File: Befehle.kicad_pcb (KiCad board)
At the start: 2 copper layers, 60 parts, among them J1 2PinTerminalBlocktg, J2 2PinTerminalBlocktg, J3 3PinTerminalBlocktg, J4 2PinTerminalBlocktg, J5 2PinTerminalBlocktg, P1 CONN_02X10, P2 CONN_02X10, U1 74LS14, U2 74540, U3 7400, U4 74HCT02, U5 74LS541, U6 74LS373, U7 74LS139, U8 74LS540

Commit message: tracks gelegt und so
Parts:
- moved R8 77.0 mm to (71.0, 109.0), turned to 0 degrees
- moved R2 76.1 mm to (146.0, 148.5)
- moved D3 1.80 mm to (73.5, 113.0), turned to 180 degrees
- moved P1 1.77 mm to (50.8, 171.8)
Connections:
- P1 pad 10: Net-(P1-Pad10) -> GND
- P1 pad 11: Net-(P1-Pad11) -> GND
- P1 pad 12: GND -> /d2
- P1 pad 13: Net-(P1-Pad13) -> /d1
- P1 pad 14: Net-(P1-Pad14) -> /d2
- P1 pad 15: Net-(P1-Pad15) -> /d3
- P1 pad 16: Net-(P1-Pad16) -> /d4
- P1 pad 3: Net-(P1-Pad3) -> GND
- P1 pad 4: Net-(P1-Pad4) -> GND
- P1 pad 5: Net-(P1-Pad5) -> GND
- P1 pad 6: Net-(P1-Pad6) -> GND
- P1 pad 7: Net-(P1-Pad7) -> GND
- P1 pad 8: Net-(P1-Pad8) -> GND
- P1 pad 9: Net-(P1-Pad9) -> GND
- U5 pad 7: /a6 -> /a4
- U6 pad 11: Net-(U6-Pad11) -> Net-(R8-Pad2)
- U6 pad 15: /a3 -> /a4
- U6 pad 16: Net-(U6-Pad16) -> /a8
- U6 pad 19: Net-(U6-Pad19) -> /a2
- U6 pad 2: /a8 -> /a1
- U6 pad 3: /11 -> /d2
- U6 pad 5: /a7 -> /a3
- U6 pad 6: /a6 -> /a5
- U6 pad 9: /a5 -> /a7
- U7 pad 2: Net-(U6-Pad19) -> /a7
- U7 pad 3: Net-(U6-Pad16) -> /a4
- U8 pad 4: /a6 -> /a4
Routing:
- net GND: track 453.5 -> 565.5 mm, vias 0 -> 2
- net loadIR: track 22.8 -> 100.2 mm, vias 0 -> 2
- net Net-(R8-Pad2): track 0.00 -> 66.4 mm
- net /a4: track 80.4 -> 144.2 mm, vias 0 -> 2
- net /a6: track 41.1 -> 0.00 mm, vias 2 -> 0
- net /a5: track 49.3 -> 76.2 mm
- net /a3: track 67.8 -> 91.1 mm
- net /a1: track 87.5 -> 104.0 mm
- net /d2: track 17.1 -> 33.2 mm
- net /a8: track 58.8 -> 74.7 mm
- net /a2: track 77.9 -> 89.6 mm
- net Net-(D3-Pad2): track 0.00 -> 4.02 mm
- net /d3: track 36.9 -> 33.4 mm
- net /a7: track 86.8 -> 90.1 mm

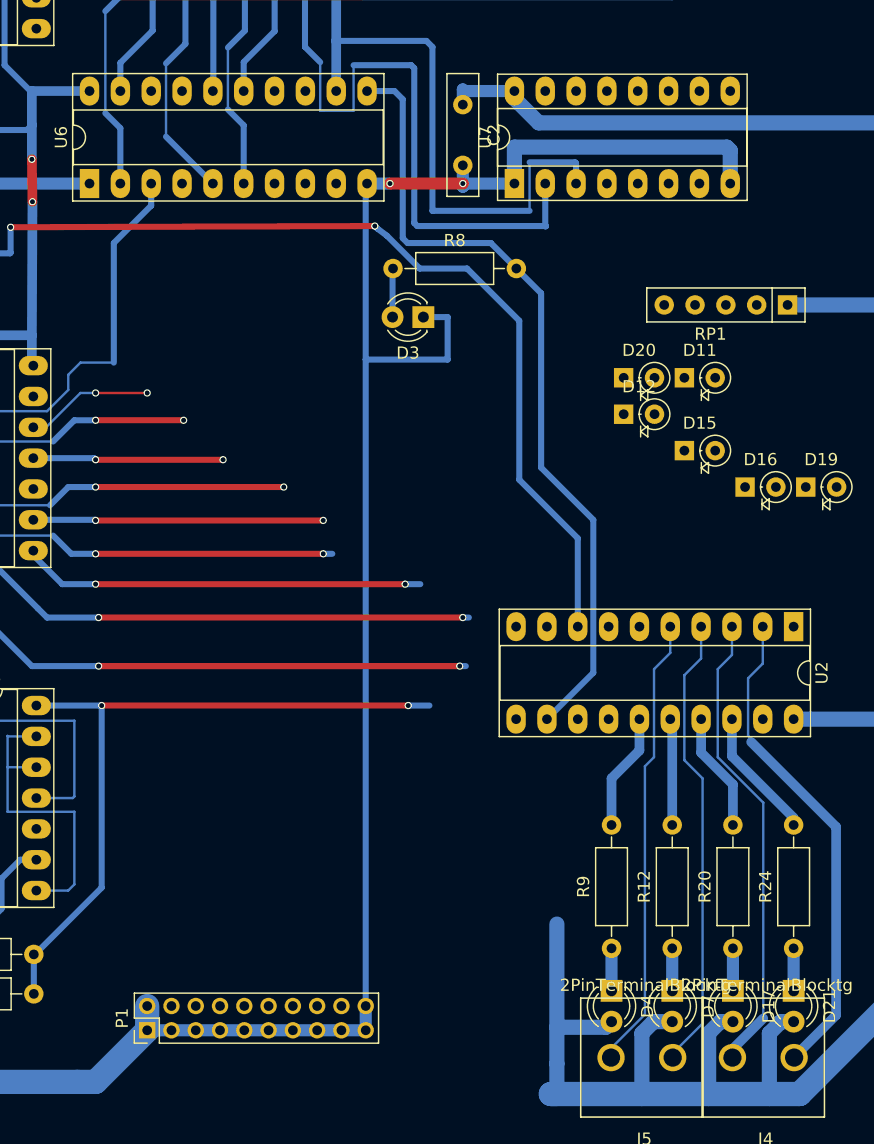
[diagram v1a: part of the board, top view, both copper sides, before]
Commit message: todos done (netze entflechten), some footprintslocaliszed
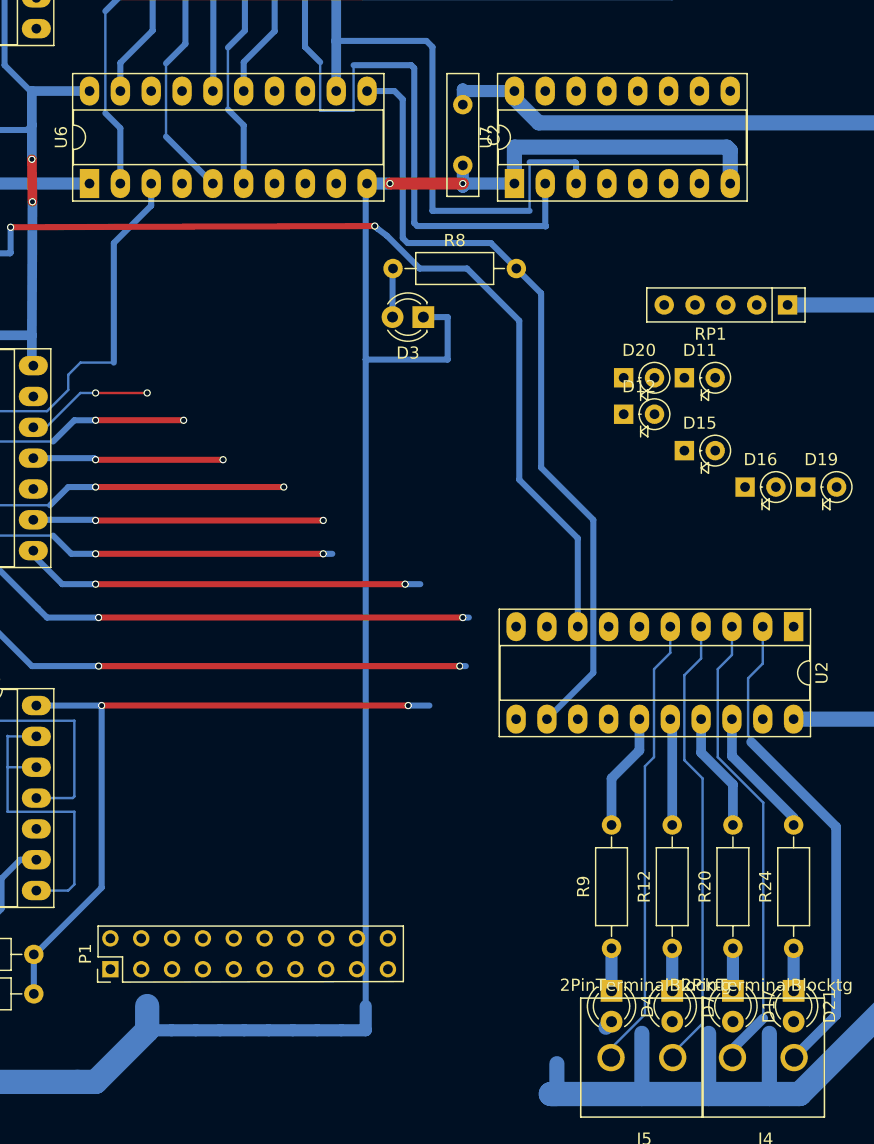
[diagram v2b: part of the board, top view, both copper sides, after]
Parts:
- U1, U3, U4: footprint Housings_DIP:DIP-14_W7.62mm_Socket_LongPads -> tg_foodprint:DIP-14_W7.62mm_Socket_LongPadstg
- U2, U5, U6, U8: footprint Housings_DIP:DIP-20_W7.62mm_Socket_LongPads -> tg_foodprint:DIP-20_W7.62mm_Socket_LongPadstg
- U7: footprint Housings_DIP:DIP-16_W7.62mm_Socket_LongPads -> tg_foodprint:DIP-16_W7.62mm_Socket_LongPadstg
- moved P1 5.87 mm to (47.7, 166.7)
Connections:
- P1 pad 12: /d2 -> (no net)
- P2 pad 11: Net-(P2-Pad11) -> (no net)
- P2 pad 12: Net-(P2-Pad12) -> (no net)
- P2 pad 13: Net-(P2-Pad13) -> (no net)
- P2 pad 14: Net-(P2-Pad14) -> (no net)
- P2 pad 15: Net-(P2-Pad15) -> (no net)
- P2 pad 16: Net-(P2-Pad16) -> (no net)
- P2 pad 17: Net-(P2-Pad17) -> (no net)
- P2 pad 18: Net-(P2-Pad18) -> (no net)
- U1 pad 8: Net-(U1-Pad8) -> (no net)
- U4 pad 10: Net-(U4-Pad10) -> (no net)
- U4 pad 11: /11 -> (no net)
- U4 pad 13: Net-(U4-Pad13) -> (no net)
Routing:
- net /11: track 15.7 -> 0.00 mm, vias 2 -> 0
- net (no net): track 0.00 -> 15.7 mm, vias 0 -> 2
- net VCC: track 607.2 -> 591.6 mm
- net Net-(D17-Pad2): track 8.31 -> 0.65 mm

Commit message: wires gelegt und schamdoozels beseitigt
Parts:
- moved R2 122.5 mm to (25.1, 129.3), turned to 270 degrees
- moved P1 5.20 mm to (45.8, 171.6)
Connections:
- J3 pad 2: incPCz -> incPC
- P1 pad 12: (no net) -> /d2
- P1 pad 14: /d2 -> /d7
- P1 pad 16: /d4 -> /d44
- P1 pad 19: /d7 -> /d4
- P2 pad 11: (no net) -> Net-(P2-Pad11)
- P2 pad 12: (no net) -> Net-(P2-Pad12)
- P2 pad 13: (no net) -> Net-(P2-Pad13)
- P2 pad 14: (no net) -> Net-(P2-Pad14)
- P2 pad 15: (no net) -> Net-(P2-Pad15)
- P2 pad 16: (no net) -> Net-(P2-Pad16)
- P2 pad 17: (no net) -> Net-(P2-Pad17)
- P2 pad 18: (no net) -> Net-(P2-Pad18)
- R3 pad 1: incPCz -> incPC
- R7 pad 1: Net-(R7-Pad1) -> incPC
- U1 pad 8: (no net) -> Net-(U1-Pad8)
- U2 pad 9: Net-(R7-Pad1) -> incPC
- U3 pad 1: incPCz -> incPC
- U3 pad 10: Net-(U3-Pad10) -> incPC
- U3 pad 2: incPCz -> incPC
- U3 pad 3: Net-(U3-Pad3) -> incPC
- U3 pad 4: Net-(R7-Pad1) -> incPC
- U3 pad 5: Net-(U3-Pad3) -> incPC
- U3 pad 6: Net-(U3-Pad10) -> incPC
- U4 pad 1: Net-(R7-Pad1) -> incPC
- U4 pad 10: (no net) -> incPC
- U4 pad 11: (no net) -> /d3
- U4 pad 12: /d7 -> /d1
- U4 pad 13: (no net) -> incPC
- U4 pad 3: /d1 -> /d7
- U4 pad 4: Net-(R7-Pad1) -> incPC
- U4 pad 5: /d4 -> /d44
- U4 pad 6: /d3 -> /d6
- U4 pad 8: /d6 -> /d4
- U6 pad 14: /d3 -> /d5
- U6 pad 17: /d2 -> /d3
- U6 pad 7: /d6 -> /d44
- U6 pad 8: /d5 -> /d6
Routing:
- net incPC: track 28.6 -> 225.0 mm, vias 0 -> 2
- net /d44: track 0.00 -> 94.2 mm, vias 0 -> 2
- net /d7: track 9.91 -> 88.0 mm
- net /d4: track 29.4 -> 103.1 mm
- net /d5: track 23.9 -> 95.7 mm
- net Net-(R7-Pad1): track 70.1 -> 0.00 mm, vias 2 -> 0
- net /d6: track 33.2 -> 98.3 mm
- net /d1: track 21.2 -> 85.7 mm
- net Net-(D1-Pad1): track 66.1 -> 3.32 mm, vias 4 -> 0
- net Net-(R2-Pad2): track 0.00 -> 59.1 mm, vias 0 -> 2
- net /d3: track 33.4 -> 91.5 mm
- net /d2: track 33.2 -> 85.6 mm
- net VCC: track 591.6 -> 625.6 mm
- net (no net): track 15.7 -> 0.00 mm, vias 2 -> 0
- net GND: track 565.5 -> 581.0 mm, vias 2 -> 4
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
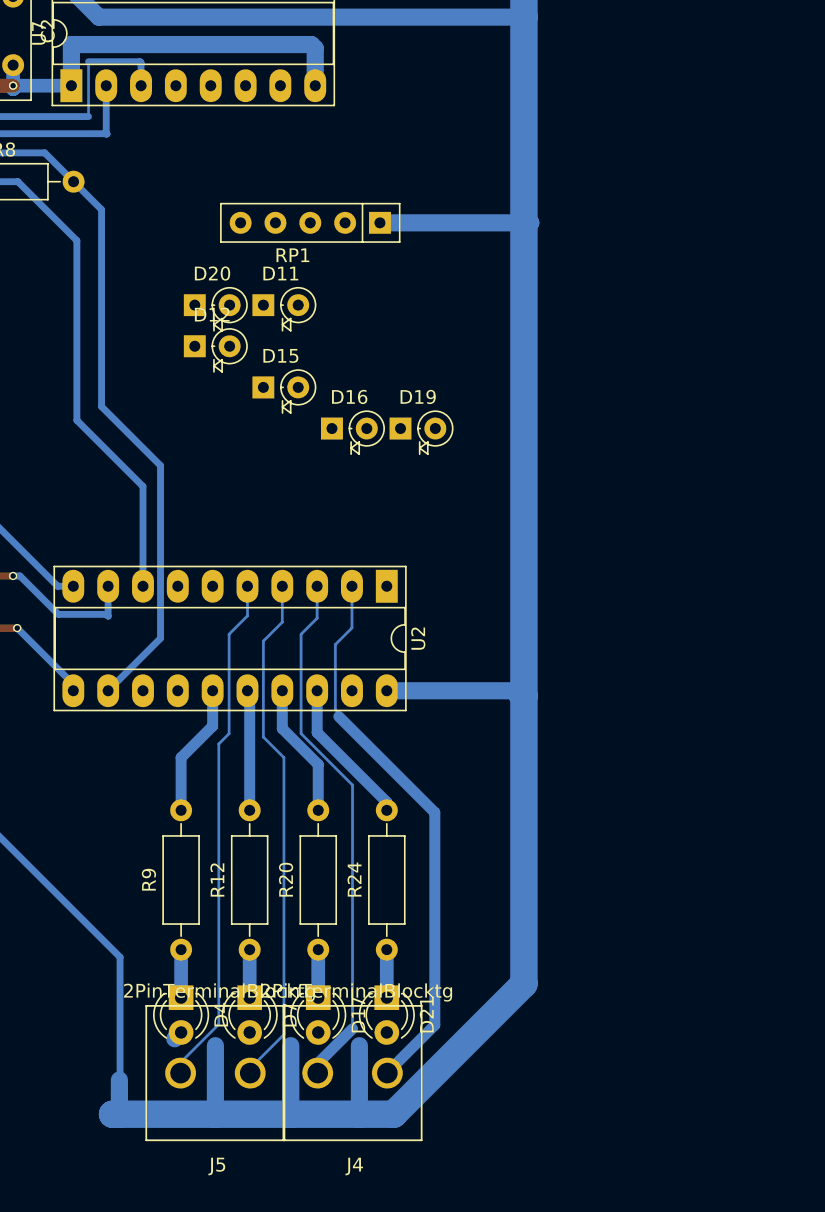
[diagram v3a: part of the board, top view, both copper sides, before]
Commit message: wires gelegt footprints getauscht
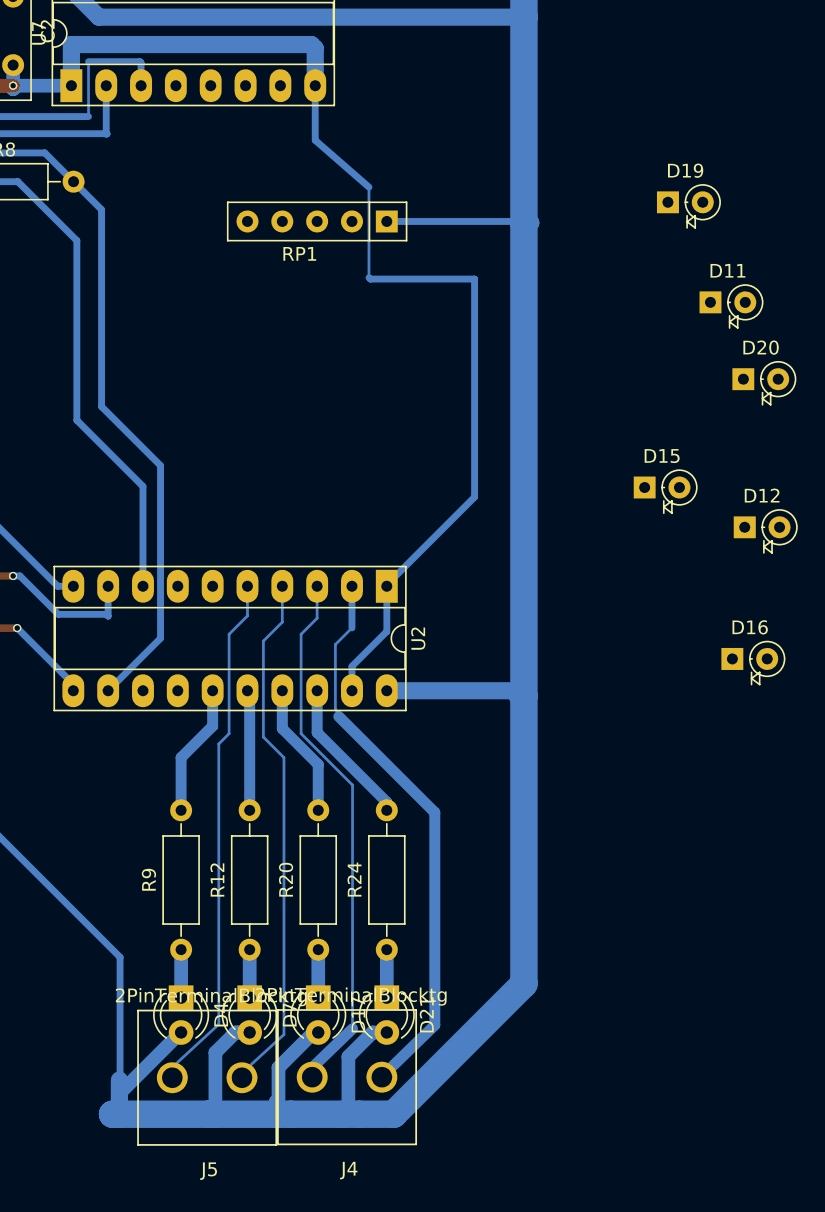
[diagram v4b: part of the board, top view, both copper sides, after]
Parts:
- moved D12 42.2 mm to (130.1, 134.2)
- moved D20 40.4 mm to (130.0, 123.4)
- moved D16 33.7 mm to (129.2, 143.8)
- moved D11 32.6 mm to (127.6, 117.8)
- moved D15 28.7 mm to (122.8, 131.3)
- moved D19 25.5 mm to (124.5, 110.5)
- moved J5 0.69 mm to (90.9, 174.3)
- moved RP1 0.51 mm to (104.0, 111.9)
- moved J4 0.50 mm to (101.1, 174.3)
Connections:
- D17 pad 2: Net-(D17-Pad2) -> VCC
- D21 pad 2: Net-(D17-Pad2) -> VCC
- D4 pad 2: Net-(D17-Pad2) -> VCC
- D7 pad 2: Net-(D17-Pad2) -> VCC
- U2 pad 15: Net-(R9-Pad2) -> Net-(R24-Pad2)
- U2 pad 16: VCC -> Net-(R20-Pad2)
- U2 pad 17: Net-(R20-Pad2) -> VCC
- U2 pad 18: Net-(R24-Pad2) -> Net-(R9-Pad2)
- U2 pad 2: 0 -> 3
- U2 pad 3: 1 -> 2
- U2 pad 4: 2 -> 1
- U2 pad 5: 3 -> 0
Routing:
- net GND: track 581.0 -> 638.3 mm
- net VCC: track 625.6 -> 644.1 mm
- net 2: track 37.7 -> 38.4 mm
- net 3: track 37.5 -> 38.2 mm
- net Net-(D17-Pad2): track 0.65 -> 0.00 mm
- net 1: track 38.6 -> 39.1 mm
- net 0: track 40.4 -> 41.0 mm

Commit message: lololol fertig gg ez
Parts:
- D11, D12, D15, D16, D19, D20: footprint Diodes_ThroughHole:D_DO-35_SOD27_P2.54mm_Vertical_KathodeUp -> tg_foodprint:Diode_D1.8mm_W3.3mm_H2.4mmBonsai
- moved D16 38.9 mm to (96.4, 122.9)
- moved D12 38.8 mm to (93.8, 120.4)
- moved D11 33.8 mm to (93.8, 116.9)
- moved D15 30.1 mm to (96.4, 116.9)
- moved D19 29.6 mm to (98.9, 125.4)
- moved D20 28.6 mm to (101.5, 125.4)
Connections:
- RP1 pad 2: 3 -> 0
- RP1 pad 3: 2 -> 1
- RP1 pad 4: 1 -> 2
- RP1 pad 5: 0 -> 3
- U2 pad 2: 3 -> 0
- U2 pad 3: 2 -> 1
- U2 pad 4: 1 -> 2
- U2 pad 5: 0 -> 3
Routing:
- net Net-(D19-Pad2): track 0.00 -> 47.8 mm, vias 0 -> 2
- net Net-(D16-Pad2): track 0.00 -> 46.1 mm, vias 0 -> 2
- net Net-(D12-Pad2): track 0.00 -> 42.4 mm, vias 0 -> 2
- net Net-(D11-Pad2): track 0.00 -> 38.2 mm, vias 0 -> 2
- net 1: track 39.1 -> 65.8 mm
- net 0: track 41.0 -> 67.6 mm
- net 3: track 38.2 -> 64.8 mm
- net 2: track 38.4 -> 65.0 mm

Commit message: bugs behoben
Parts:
- U2: footprint tg_foodprint:DIP-20_W7.62mm_Socket_LongPadstg -> Housings_DIP:DIP-20_W7.62mm_Socket_LongPads
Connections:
- J3 pad 2: incPC -> incPCz
- R12 pad 2: VCC -> Net-(R12-Pad2)
- R3 pad 1: incPC -> incPCz
- R7 pad 1: incPC -> Net-(R7-Pad1)
- U2 pad 1: GND -> Net-(U2-Pad1)
- U2 pad 15: Net-(R24-Pad2) -> Net-(R9-Pad2)
- U2 pad 16: Net-(R20-Pad2) -> Net-(R12-Pad2)
- U2 pad 17: VCC -> Net-(R20-Pad2)
- U2 pad 18: Net-(R9-Pad2) -> Net-(R24-Pad2)
- U2 pad 19: GND -> Net-(U2-Pad19)
- U2 pad 9: incPC -> Net-(R7-Pad1)
- U3 pad 1: incPC -> Net-(R7-Pad1)
- U3 pad 10: incPC -> Net-(U3-Pad10)
- U3 pad 2: incPC -> Net-(R7-Pad1)
- U3 pad 3: incPC -> Net-(U3-Pad10)
- U3 pad 4: incPC -> incPCz
- U3 pad 5: incPC -> incPCz
- U3 pad 6: incPC -> Net-(R7-Pad1)
- U4 pad 1: incPC -> Net-(R7-Pad1)
- U4 pad 10: incPC -> Net-(R7-Pad1)
- U4 pad 13: incPC -> Net-(R7-Pad1)
- U4 pad 4: incPC -> Net-(R7-Pad1)
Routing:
- net incPC: track 225.0 -> 28.6 mm, vias 2 -> 0
- net Net-(R7-Pad1): track 0.00 -> 155.7 mm, vias 0 -> 2
- net VCC: track 644.1 -> 696.2 mm, vias 4 -> 8
- net incPCz: track 0.00 -> 27.3 mm
- net Net-(U3-Pad10): track 0.00 -> 10.9 mm
- net Net-(R12-Pad2): track 0.00 -> 8.79 mm

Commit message: bugs behoben und fertig gestellt
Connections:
- P2 pad 11: Net-(P2-Pad11) -> GND
- P2 pad 12: Net-(P2-Pad12) -> GND
- P2 pad 13: Net-(P2-Pad13) -> GND
- P2 pad 14: Net-(P2-Pad14) -> GND
- P2 pad 15: Net-(P2-Pad15) -> GND
- P2 pad 16: Net-(P2-Pad16) -> GND
- P2 pad 17: Net-(P2-Pad17) -> GND
- P2 pad 18: Net-(P2-Pad18) -> GND
- U2 pad 1: Net-(U2-Pad1) -> GND
- U2 pad 19: Net-(U2-Pad19) -> GND
- U3 pad 2: Net-(R7-Pad1) -> Net-(U3-Pad2)
- U3 pad 6: Net-(R7-Pad1) -> Net-(U3-Pad2)
- U5 pad 7: /a4 -> /a6
- U6 pad 15: /a4 -> /a6
- U8 pad 4: /a4 -> /a6
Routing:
- net /a4: track 144.2 -> 82.1 mm, vias 2 -> 0
- net /a6: track 0.00 -> 62.1 mm, vias 0 -> 2
- net GND: track 638.3 -> 698.5 mm
- net Net-(U1-Pad2): track 0.00 -> 24.8 mm
- net Net-(R7-Pad1): track 155.7 -> 137.4 mm
- net Net-(U3-Pad2): track 0.00 -> 18.3 mm
- net incPCz: track 27.3 -> 29.8 mm
